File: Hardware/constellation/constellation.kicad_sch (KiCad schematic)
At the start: 1 part, among them U1 STM32H723ZGTx

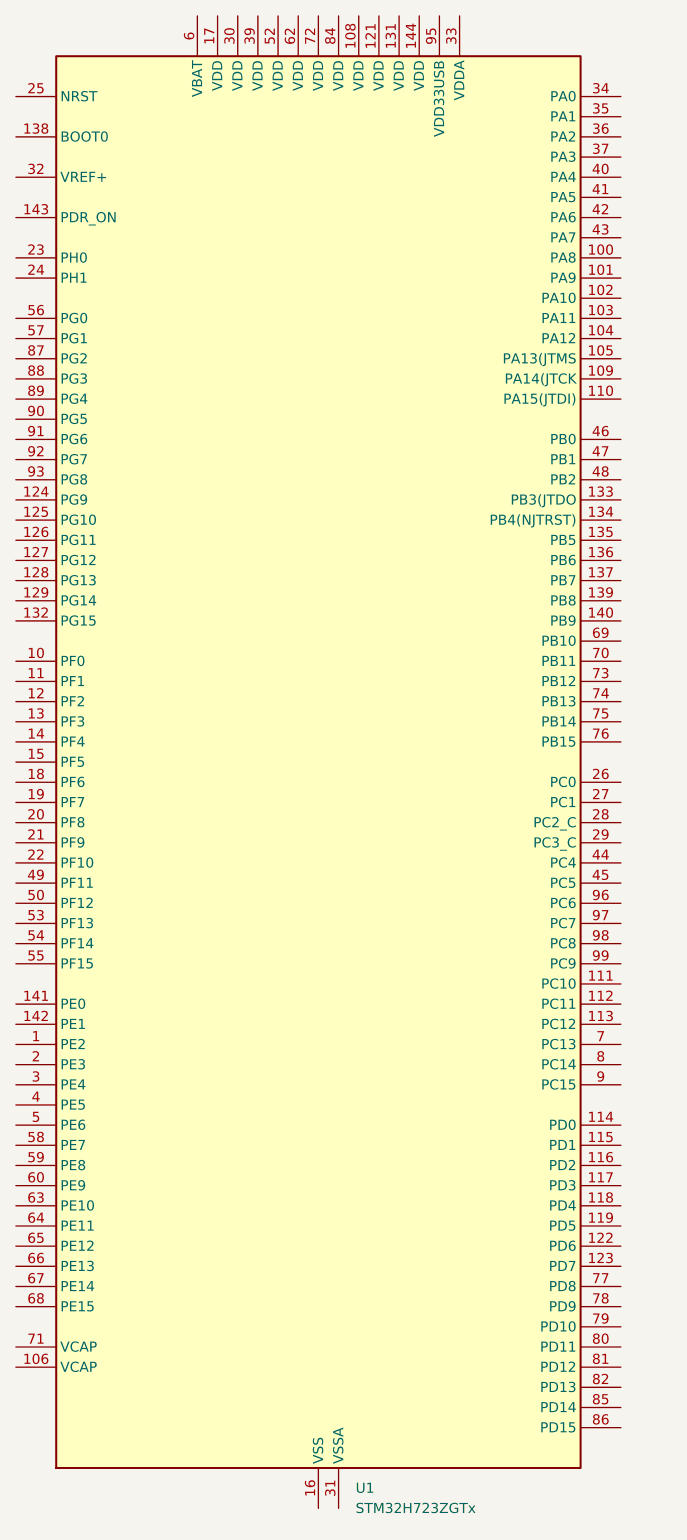
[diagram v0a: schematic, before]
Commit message: finalize baros and add the magnetometer sheet
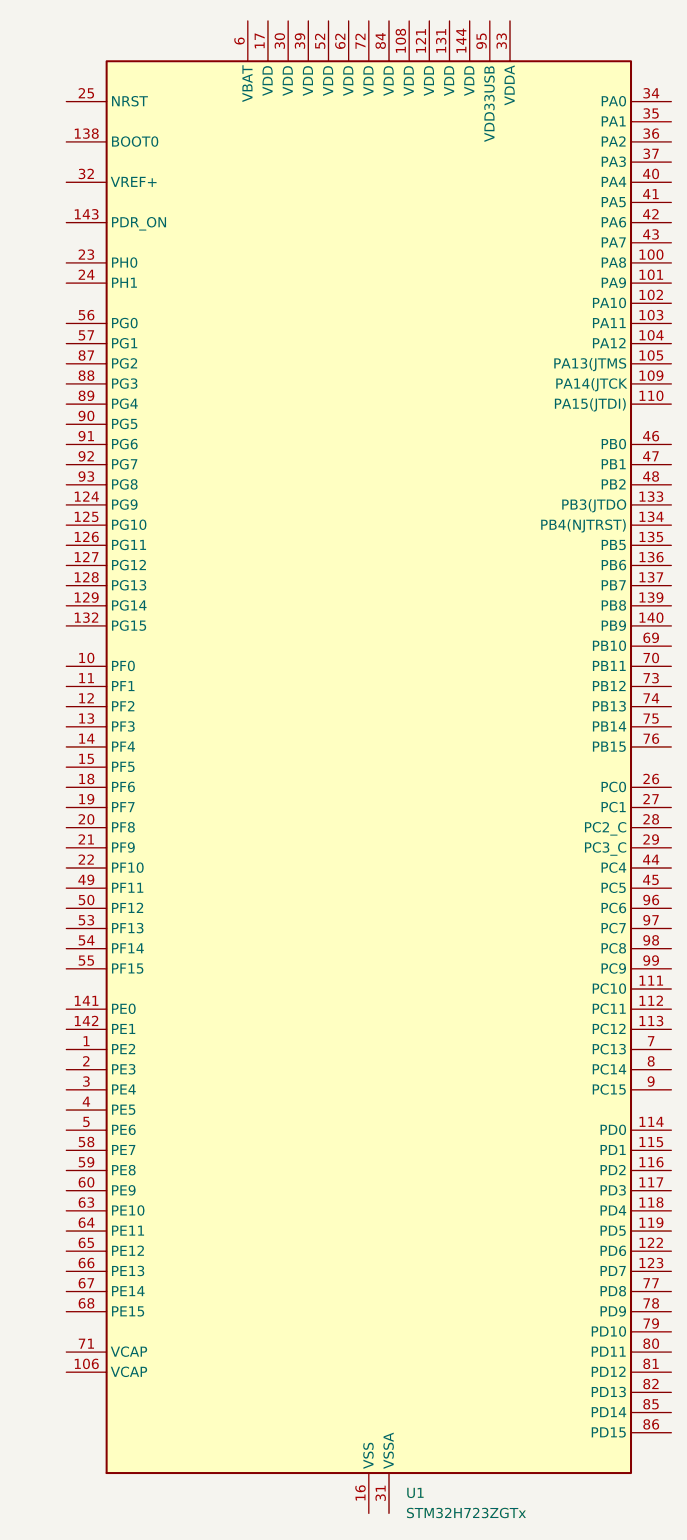
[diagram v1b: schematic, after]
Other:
- moved on the sheet: U1
